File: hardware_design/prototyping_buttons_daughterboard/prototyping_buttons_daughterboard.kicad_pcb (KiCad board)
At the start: 2 copper layers, 80 x 30.5 mm, 10 parts, among them J1 Conn_02x10_Counter_Clockwise, J2 Conn_02x10_Counter_Clockwise

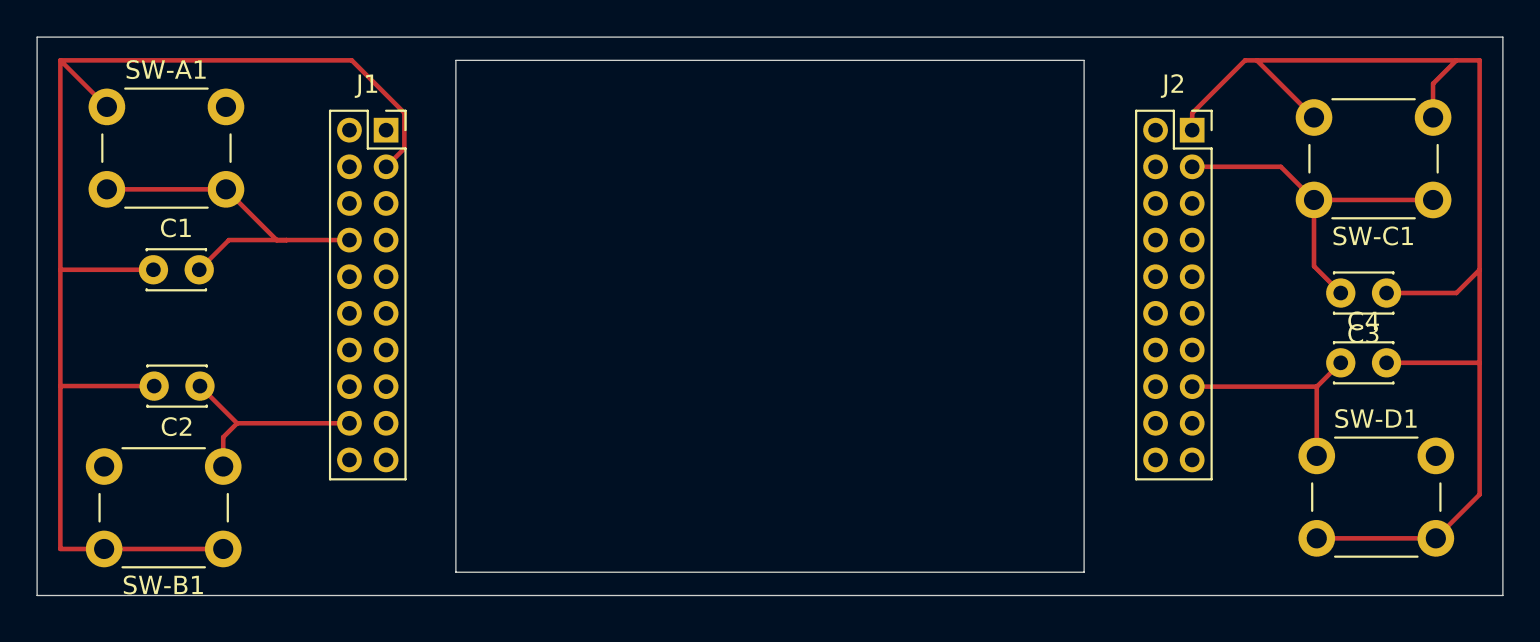
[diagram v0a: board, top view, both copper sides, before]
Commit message: Changes to be committed: 	new file:   hardware_design/README.md 	new file:   hardware_design/prototyping_buttons_daughterboard.zip 	modified:   hardware_design/prototyping_buttons_daughterboard/fp-info-cache 	modified:   hardware_design/prototyping_buttons_daughterboard/gerber/prototyping_buttons_daughterboard-B_Cu.gbr 	modified:   hardware_design/prototyping_buttons_daughterboard/gerber/prototyping_buttons_daughterboard-Edge_Cuts.gbr 	modified:   hardware_design/prototyping_buttons_daughterboard/gerber/prototyping_buttons_daughterboard-F_Cu.gbr 	modified:   hardware_design/prototyping_buttons_daughterboard/gerber/prototyping_buttons_daughterboard-NPTH.drl 	modified:   hardware_design/prototyping_buttons_daughterboard/gerber/prototyping_buttons_daughterboard-PTH.drl 	modified:   hardware_design/prototyping_buttons_daughterboard/prototyping_buttons_daughterboard.kicad_pcb 	modified:   hardware_design/prototyping_buttons_daughterboard/prototyping_buttons_daughterboard.kicad_pcb-bak 	modified:   hardware_design/prototyping_buttons_daughterboard/prototyping_buttons_daughterboard.pro
Modifications represent thickening traces for the daughterboard design at the request of the prototyper, to suit their manufacturing requirements.
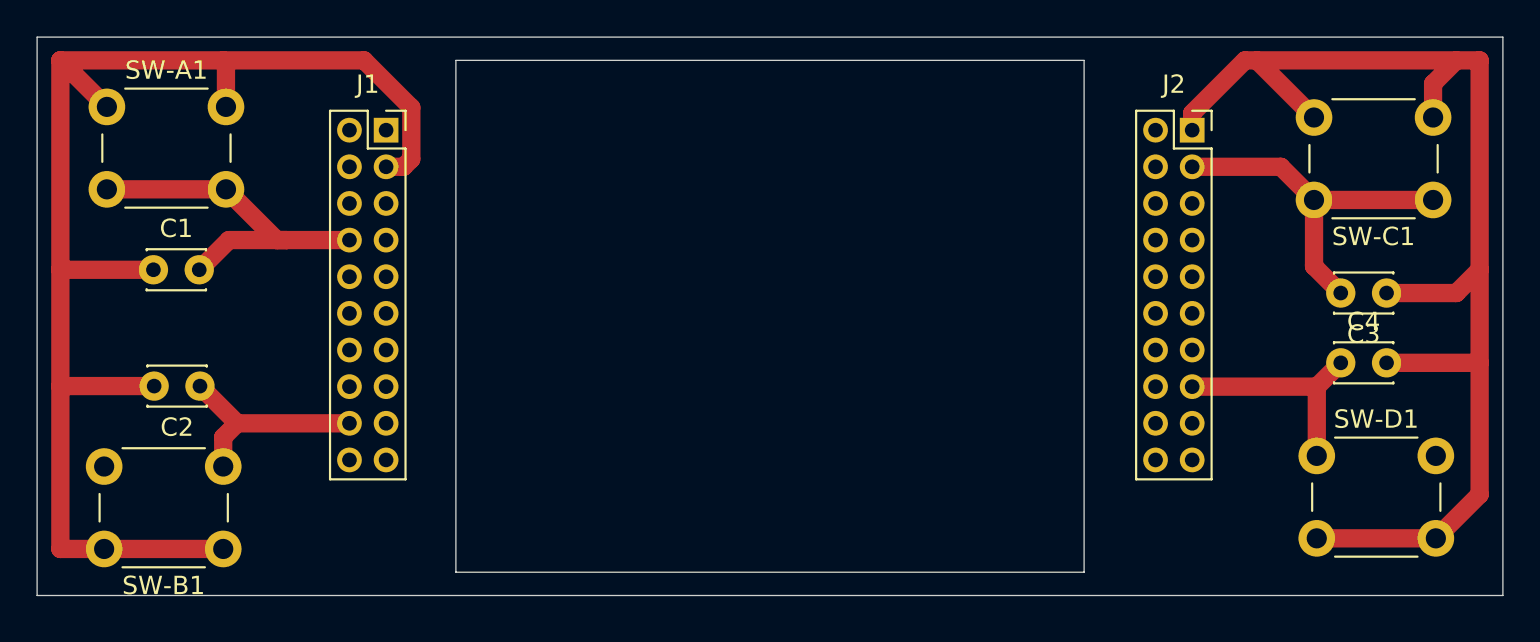
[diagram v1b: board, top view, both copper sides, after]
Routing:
- net Net-(C1-Pad1): track 72.7 -> 76.5 mm
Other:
- net class Default: trace_width 0.25 -> 1
- rule trace_min: 0.2 -> 1
